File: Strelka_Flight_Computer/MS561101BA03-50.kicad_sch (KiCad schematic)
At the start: 2 parts, among them U12 MS561101BA03-50

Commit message: Changed design rules
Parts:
- C30: footprint Capacitor_SMD:C_0603_1608Metric -> Capacitor_SMD:C_0402_1005Metric
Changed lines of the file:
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@@
       (effects (font (size 1.27 1.27)) (justify left))
     )
-    (property "Footprint" "Capacitor_SMD:C_0603_1608Metric" (at 104.775 94.615 0)
+    (property "Footprint" "Capacitor_SMD:C_0402_1005Metric" (at 104.775 94.615 0)
       (effects (font (size 1.27 1.27)) hide)
     )

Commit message: Continued routing
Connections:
- net +3V3 renamed +3.3V
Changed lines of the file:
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@@
+    )
+  )
+  (symbol (lib_name "+3.3V_1") (lib_id "power:+3.3V") (at 104.775 87.63 0) (unit 1)
+    (in_bom yes) (on_board yes) (dnp no) (fields_autoplaced)
+    (property "Reference" "#PWR07" (at 104.775 91.44 0)
+      (effects (font (size 1.27 1.27)) hide)
+    )
+    (property "Value" "+3.3V" (at 104.775 84.455 0)
+      (effects (font (size 1.27 1.27)))
+    )
+    (property "Footprint" "" (at 104.775 87.63 0)
+      (effects (font (size 1.27 1.27)) hide)
+    )
+    (property "Datasheet" "" (at 104.775 87.63 0)
+      (effects (font (size 1.27 1.27)) hide)
+    )
+    (pin "1")
+    (instances
+      (project "Strelka_Flight_Computer"
+        (path "/e63e39d7-6ac0-4ffd-8aa3-1841a4541b55/e94c6cea-6c6c-4b5f-a840-b97a15d9406a"
+          (reference "#PWR07") (unit 1)
+        )
+        (path "/e63e39d7-6ac0-4ffd-8aa3-1841a4541b55/78f71895-bddb-4f64-a608-99074f2d1c44/9f95701d-2876-4223-990f-d706d5845c81"
+          (reference "#PWR010") (unit 1)
+        )
+      )
     )
   )
@@
     )
   )
-  (symbol (lib_id "power:+3.3V") (at 104.775 87.63 0) (unit 1)
+  (symbol (lib_name "+3.3V_1") (lib_id "power:+3.3V") (at 123.825 88.265 0) (unit 1)
     (in_bom yes) (on_board yes) (dnp no) (fields_autoplaced)
-    (property "Reference" "#PWR0178" (at 104.775 91.44 0)
+    (property "Reference" "#PWR07" (at 123.825 92.075 0)
       (effects (font (size 1.27 1.27)) hide)
     )
-    (property "Value" "+3.3V" (at 104.775 84.0542 0)
+    (property "Value" "+3.3V" (at 123.825 85.09 0)
       (effects (font (size 1.27 1.27)))
     )
-    (property "Footprint" "" (at 104.775 87.63 0)
+    (property "Footprint" "" (at 123.825 88.265 0)
       (effects (font (size 1.27 1.27)) hide)
     )
-    (property "Datasheet" "" (at 104.775 87.63 0)
+    (property "Datasheet" "" (at 123.825 88.265 0)
       (effects (font (size 1.27 1.27)) hide)
     )
@@
     (instances
       (project "Strelka_Flight_Computer"
+        (path "/e63e39d7-6ac0-4ffd-8aa3-1841a4541b55/e94c6cea-6c6c-4b5f-a840-b97a15d9406a"
+          (reference "#PWR07") (unit 1)
+        )
         (path "/e63e39d7-6ac0-4ffd-8aa3-1841a4541b55/78f71895-bddb-4f64-a608-99074f2d1c44/9f95701d-2876-4223-990f-d706d5845c81"
-          (reference "#PWR0178") (unit 1)
+          (reference "#PWR03") (unit 1)
         )
       )
@@
         )
       )
-    )
-  )
-  (symbol (lib_id "power:+3.3V") (at 123.825 88.265 0) (unit 1)
-    (in_bom yes) (on_board yes) (dnp no) (fields_autoplaced)
-    (property "Reference" "#PWR0181" (at 123.825 92.075 0)
-      (effects (font (size 1.27 1.27)) hide)
-    )
-    (property "Value" "+3.3V" (at 123.825 84.6892 0)
-      (effects (font (size 1.27 1.27)))
-    )
-    (property "Footprint" "" (at 123.825 88.265 0)
-      (effects (font (size 1.27 1.27)) hide)
-    )
-    (property "Datasheet" "" (at 123.825 88.265 0)
-      (effects (font (size 1.27 1.27)) hide)
-    )
-    (pin "1")
-    (instances
-      (project "Strelka_Flight_Computer"
-        (path "/e63e39d7-6ac0-4ffd-8aa3-1841a4541b55/78f71895-bddb-4f64-a608-99074f2d1c44/9f95701d-2876-4223-990f-d706d5845c81"
-          (reference "#PWR0181") (unit 1)
-        )
-      )

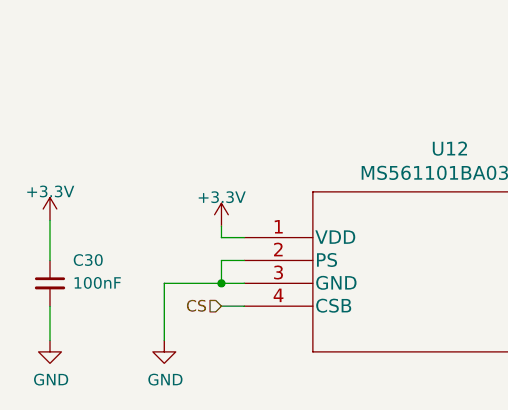
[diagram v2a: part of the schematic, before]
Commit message: Created BOM
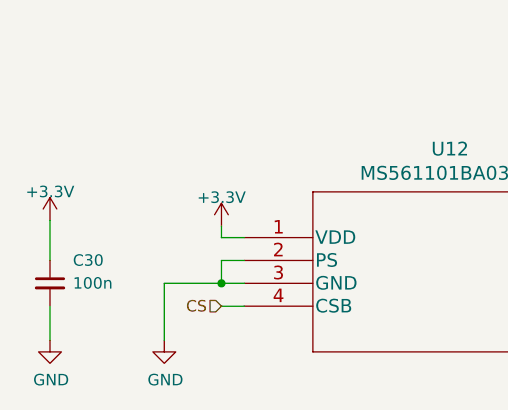
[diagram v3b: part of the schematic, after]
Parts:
- C30: value 100nF -> 100n
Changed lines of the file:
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@@
       (effects (font (size 1.27 1.27)) (justify left))
     )
-    (property "Value" "100nF" (at 107.315 94.615 0)
+    (property "Value" "100n" (at 107.315 94.615 0)
       (effects (font (size 1.27 1.27)) (justify left))
     )

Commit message: Added LCSC mpn to all relevent parts
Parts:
- C30: LCSC (none) -> C1525
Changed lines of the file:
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@@
+      (effects (font (size 1.27 1.27)) hide)
+    )
+    (property "LCSC" " C1525" (at 104.775 94.615 0)
       (effects (font (size 1.27 1.27)) hide)
     )
